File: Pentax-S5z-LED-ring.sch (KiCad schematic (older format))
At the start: 44 parts, among them IC1 ATTINY13-S, P1 CONN_2, P2 +, P3 -, P4 CONN_2, Q1 MOSFET_N, SW1 SW_PUSH, SW2 SW_PUSH

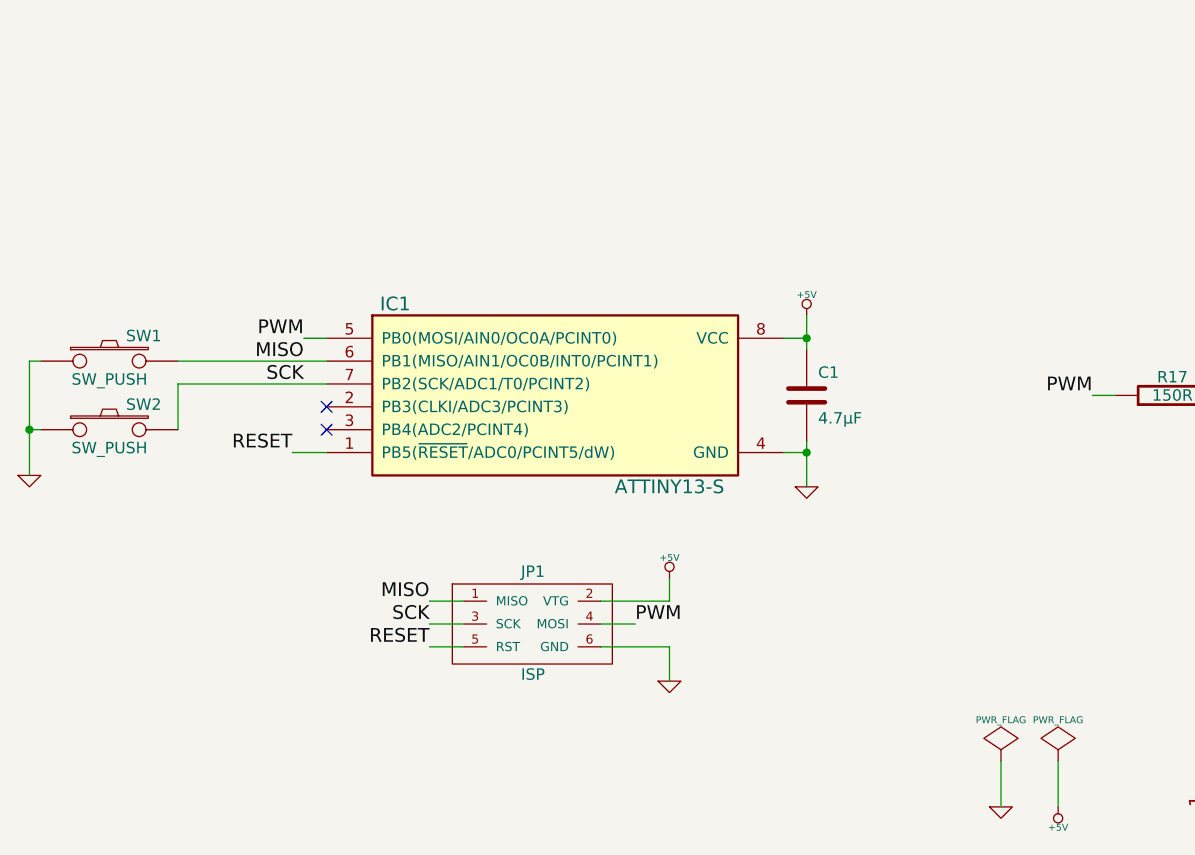
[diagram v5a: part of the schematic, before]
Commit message: Added 1k resistors for the pull-down switches. Just in case ;-)
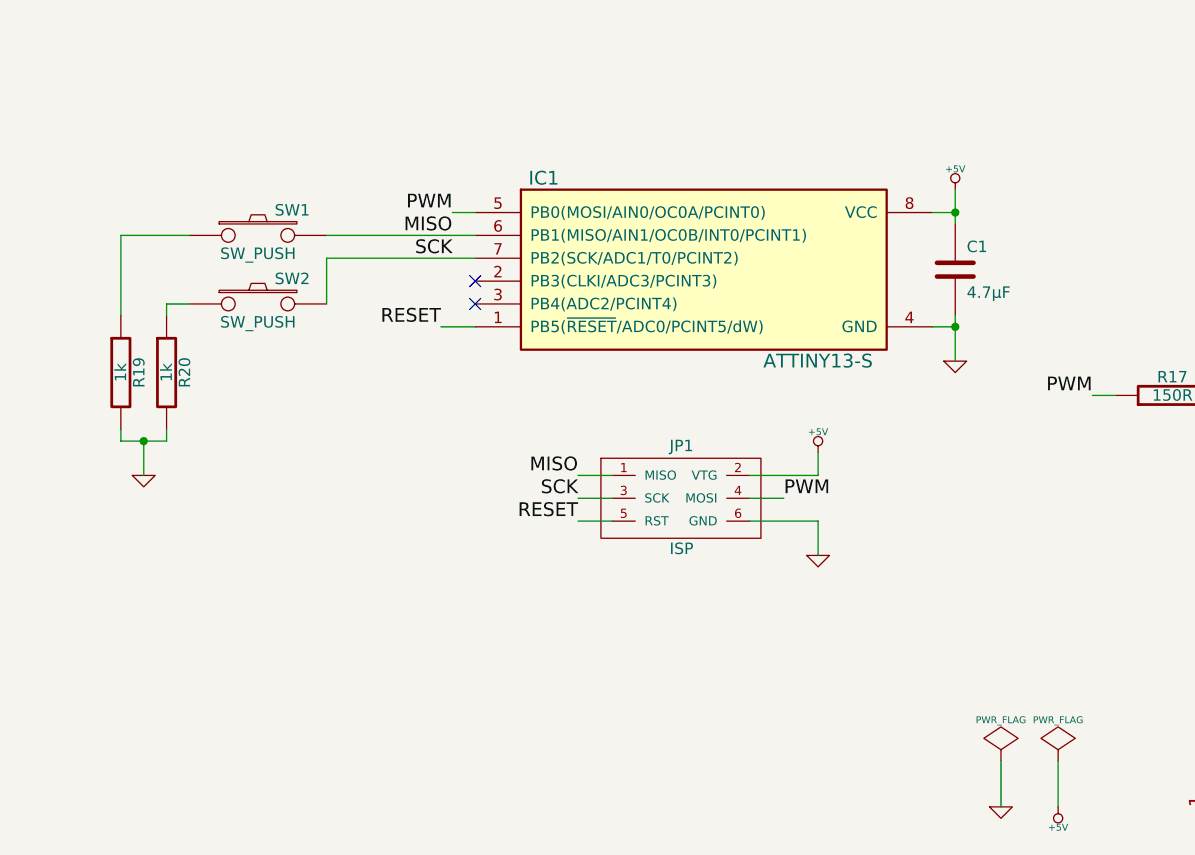
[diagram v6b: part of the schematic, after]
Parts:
- added R19, R20: 1k, symbol R
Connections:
- net GND: now also R19.2, R20.2; no longer SW1.1, SW2.1
- new net: R19.1, SW1.1
- new net: R20.1, SW2.1
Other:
- moved on the sheet: C1, IC1, JP1, SW1, SW2
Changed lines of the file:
@@
-EESchema Schematic File Version 2  date Wed 10 Apr 2013 12:16:09 AM CEST
+EESchema Schematic File Version 2  date Wed 10 Apr 2013 07:53:54 PM CEST
 LIBS:my_parts
 LIBS:power
@@
 Sheet 1 1
 Title "Pentax S5z LED ring"
-Date "9 apr 2013"
-Rev "0.1"
+Date "10 apr 2013"
+Rev "1.0"
 Comp "2013 - blog.spitzenpfeil.org"
 Comment1 ""
@@
 L ATTINY13-S IC1
 U 1 1 51640F05
-P 2500 4100
-F 0 "IC1" H 2600 4150 60  0000 C CNN
-F 1 "ATTINY13-S" H 3800 3350 60  0000 C CNN
-F 2 "SO8-200" H 2750 3350 60  0001 C CNN
-F 3 "" H 2500 4100 60  0000 C CNN
-	1    2500 4100
+P 3150 3550
+F 0 "IC1" H 3250 3600 60  0000 C CNN
+F 1 "ATTINY13-S" H 4450 2800 60  0000 C CNN
+F 2 "SO8-200" H 3400 2800 60  0001 C CNN
+F 3 "" H 3150 3550 60  0000 C CNN
+	1    3150 3550
 	1    0    0    -1
 $EndComp
@@
 L +5V #PWR04
 U 1 1 516412DB
-P 4400 4100
-F 0 "#PWR04" H 4400 4190 20  0001 C CNN
-F 1 "+5V" H 4400 4190 30  0000 C CNN
-F 2 "" H 4400 4100 60  0000 C CNN
-F 3 "" H 4400 4100 60  0000 C CNN
-	1    4400 4100
-	1    0    0    -1
-$EndComp
-Wire Wire Line
-	4400 4100 4400 4250
+P 5050 3550
+F 0 "#PWR04" H 5050 3640 20  0001 C CNN
+F 1 "+5V" H 5050 3640 30  0000 C CNN
+F 2 "" H 5050 3550 60  0000 C CNN
+F 3 "" H 5050 3550 60  0000 C CNN
+	1    5050 3550
+	1    0    0    -1
+$EndComp
+Wire Wire Line
+	5050 3550 5050 3700
 $Comp
 L GND #PWR05
 U 1 1 51641344
-P 4400 4850
-F 0 "#PWR05" H 4400 4850 30  0001 C CNN
-F 1 "GND" H 4400 4780 30  0001 C CNN
-F 2 "" H 4400 4850 60  0000 C CNN
-F 3 "" H 4400 4850 60  0000 C CNN
-	1    4400 4850
-	1    0    0    -1
-$EndComp
-Wire Wire Line
-	4400 4650 4400 4850
+P 5050 4300
+F 0 "#PWR05" H 5050 4300 30  0001 C CNN
+F 1 "GND" H 5050 4230 30  0001 C CNN
+F 2 "" H 5050 4300 60  0000 C CNN
+F 3 "" H 5050 4300 60  0000 C CNN
+	1    5050 4300
+	1    0    0    -1
+$EndComp
+Wire Wire Line
+	5050 4100 5050 4300
 Text Label 5650 4450 2    60   ~ 0
 PWM
 Wire Wire Line
 	5650 4450 5750 4450
-Text Label 2200 4200 2    60   ~ 0
+Text Label 2850 3650 2    60   ~ 0
 PWM
 Wire Wire Line
-	2200 4200 2300 4200
+	2850 3650 2950 3650
 $Comp
 L SW_PUSH SW1
 U 1 1 5164146F
-P 1350 4300
-F 0 "SW1" H 1500 4410 50  0000 C CNN
-F 1 "SW_PUSH" H 1350 4220 50  0000 C CNN
-F 2 "" H 1350 4300 60  0000 C CNN
-F 3 "" H 1350 4300 60  0000 C CNN
-	1    1350 4300
-	1    0    0    -1
-$EndComp
-$Comp
-L SW_PUSH SW2
-U 1 1 5164147E
-P 1350 4600
-F 0 "SW2" H 1500 4710 50  0000 C CNN
-F 1 "SW_PUSH" H 1350 4520 50  0000 C CNN
-F 2 "" H 1350 4600 60  0000 C CNN
-F 3 "" H 1350 4600 60  0000 C CNN
-	1    1350 4600
+P 2000 3750
+F 0 "SW1" H 2150 3860 50  0000 C CNN
+F 1 "SW_PUSH" H 2000 3670 50  0000 C CNN
+F 2 "" H 2000 3750 60  0000 C CNN
+F 3 "" H 2000 3750 60  0000 C CNN
+	1    2000 3750
 	1    0    0    -1
 $EndComp
@@
 L GND #PWR06
 U 1 1 5164148D
-P 1000 4800
-F 0 "#PWR06" H 1000 4800 30  0001 C CNN
-F 1 "GND" H 1000 4730 30  0001 C CNN
-F 2 "" H 1000 4800 60  0000 C CNN
-F 3 "" H 1000 4800 60  0000 C CNN
-	1    1000 4800
-	1    0    0    -1
-$EndComp
-Wire Wire Line
-	1050 4300 1000 4300
-Wire Wire Line
-	1000 4300 1000 4800
-Wire Wire Line
-	1000 4600 1050 4600
-Connection ~ 1000 4600
-Wire Wire Line
-	2300 4300 1650 4300
-Wire Wire Line
-	2300 4400 1650 4400
-Wire Wire Line
-	1650 4400 1650 4600
+P 1500 4800
+F 0 "#PWR06" H 1500 4800 30  0001 C CNN
+F 1 "GND" H 1500 4730 30  0001 C CNN
+F 2 "" H 1500 4800 60  0000 C CNN
+F 3 "" H 1500 4800 60  0000 C CNN
+	1    1500 4800
+	1    0    0    -1
+$EndComp
+Wire Wire Line
+	2950 3750 2300 3750
+Wire Wire Line
+	2950 3850 2300 3850
+Wire Wire Line
+	2300 3850 2300 4050
 $Comp
 L MADW__AVR_ISP JP1
 U 1 1 5164175A
-P 3200 5450
-F 0 "JP1" H 3150 5650 50  0000 L BNN
-F 1 "ISP" H 3150 5200 50  0000 L BNN
-F 2 "~" H 3200 5450 60  0000 C CNN
-F 3 "~" H 3200 5450 60  0000 C CNN
-	1    3200 5450
-	1    0    0    -1
-$EndComp
-Wire Wire Line
-	2900 5350 2750 5350
-Wire Wire Line
-	2750 5450 2900 5450
-Wire Wire Line
-	2900 5550 2750 5550
-Wire Wire Line
-	3500 5350 3800 5350
-Wire Wire Line
-	3500 5450 3650 5450
-Wire Wire Line
-	3500 5550 3800 5550
+P 3850 4900
+F 0 "JP1" H 3800 5100 50  0000 L BNN
+F 1 "ISP" H 3800 4650 50  0000 L BNN
+F 2 "~" H 3850 4900 60  0000 C CNN
+F 3 "~" H 3850 4900 60  0000 C CNN
+	1    3850 4900
+	1    0    0    -1
+$EndComp
+Wire Wire Line
+	3550 4800 3400 4800
+Wire Wire Line
+	3400 4900 3550 4900
+Wire Wire Line
+	3550 5000 3400 5000
+Wire Wire Line
+	4150 4800 4450 4800
+Wire Wire Line
+	4150 4900 4300 4900
+Wire Wire Line
+	4150 5000 4450 5000
 $Comp
 L GND #PWR07
 U 1 1 516419E6
-P 3800 5700
-F 0 "#PWR07" H 3800 5700 30  0001 C CNN
-F 1 "GND" H 3800 5630 30  0001 C CNN
-F 2 "" H 3800 5700 60  0000 C CNN
-F 3 "" H 3800 5700 60  0000 C CNN
-	1    3800 5700
+P 4450 5150
+F 0 "#PWR07" H 4450 5150 30  0001 C CNN
+F 1 "GND" H 4450 5080 30  0001 C CNN
+F 2 "" H 4450 5150 60  0000 C CNN
+F 3 "" H 4450 5150 60  0000 C CNN
+	1    4450 5150
 	1    0    0    -1
 $EndComp
@@
 L +5V #PWR08
 U 1 1 516419F5
-P 3800 5250
-F 0 "#PWR08" H 3800 5340 20  0001 C CNN
-F 1 "+5V" H 3800 5340 30  0000 C CNN
-F 2 "" H 3800 5250 60  0000 C CNN
-F 3 "" H 3800 5250 60  0000 C CNN
-	1    3800 5250
-	1    0    0    -1
-$EndComp
-Wire Wire Line
-	3800 5350 3800 5250
-Wire Wire Line
-	3800 5550 3800 5700
-Text Label 3650 5450 0    60   ~ 0
+P 4450 4700
+F 0 "#PWR08" H 4450 4790 20  0001 C CNN
+F 1 "+5V" H 4450 4790 30  0000 C CNN
+F 2 "" H 4450 4700 60  0000 C CNN
+F 3 "" H 4450 4700 60  0000 C CNN
+	1    4450 4700
+	1    0    0    -1
+$EndComp
+Wire Wire Line
+	4450 4800 4450 4700
+Wire Wire Line
+	4450 5000 4450 5150
+Text Label 4300 4900 0    60   ~ 0
 PWM
-Text Label 2750 5350 2    60   ~ 0
+Text Label 3400 4800 2    60   ~ 0
 MISO
-Text Label 2750 5450 2    60   ~ 0
+Text Label 3400 4900 2    60   ~ 0
 SCK
-Text Label 2750 5550 2    60   ~ 0
+Text Label 3400 5000 2    60   ~ 0
 RESET
-Text Label 2200 4300 2    60   ~ 0
+Text Label 2850 3750 2    60   ~ 0
 MISO
-Text Label 2200 4400 2    60   ~ 0
+Text Label 2850 3850 2    60   ~ 0
 SCK
-Text Label 2150 4700 2    60   ~ 0
+Text Label 2800 4150 2    60   ~ 0
 RESET
 Wire Wire Line
-	2150 4700 2300 4700
-NoConn ~ 2300 4500
-NoConn ~ 2300 4600
+	2800 4150 2950 4150
+NoConn ~ 2950 3950
+NoConn ~ 2950 4050
 $Comp
 L GND #PWR09
@@
 Text Notes 7150 3850 0    60   ~ 0
 To LED board
-Connection ~ 4400 4200
-Connection ~ 4400 4700
+Connection ~ 5050 3650
+Connection ~ 5050 4150
 $Comp
 L C C1
 U 1 1 516492F3
-P 4400 4450
-F 0 "C1" H 4450 4550 50  0000 L CNN
-F 1 "4.7µF" H 4450 4350 50  0000 L CNN
-F 2 "" H 4400 4450 60  0000 C CNN
-F 3 "" H 4400 4450 60  0000 C CNN
-	1    4400 4450
-	1    0    0    -1
-$EndComp
-Wire Wire Line
-	4300 4200 4400 4200
-Wire Wire Line
-	4300 4700 4400 4700
+P 5050 3900
+F 0 "C1" H 5100 4000 50  0000 L CNN
+F 1 "4.7µF" H 5100 3800 50  0000 L CNN
+F 2 "" H 5050 3900 60  0000 C CNN
+F 3 "" H 5050 3900 60  0000 C CNN
+	1    5050 3900
+	1    0    0    -1
+$EndComp
+Wire Wire Line
+	4950 3650 5050 3650
+Wire Wire Line
+	4950 4150 5050 4150
+$Comp
+L R R19
+U 1 1 5165A46F
+P 1400 4350
+F 0 "R19" V 1480 4350 50  0000 C CNN
+F 1 "1k" V 1400 4350 50  0000 C CNN
+F 2 "" H 1400 4350 60  0000 C CNN
+F 3 "" H 1400 4350 60  0000 C CNN
+	1    1400 4350
+	1    0    0    -1
+$EndComp
+$Comp
+L R R20
+U 1 1 5165A47E
+P 1600 4350
+F 0 "R20" V 1680 4350 50  0000 C CNN
+F 1 "1k" V 1600 4350 50  0000 C CNN
+F 2 "" H 1600 4350 60  0000 C CNN
+F 3 "" H 1600 4350 60  0000 C CNN
+	1    1600 4350
+	1    0    0    -1
+$EndComp
+$Comp
+L SW_PUSH SW2
+U 1 1 5164147E
+P 2000 4050
+F 0 "SW2" H 2150 4160 50  0000 C CNN
+F 1 "SW_PUSH" H 2000 3970 50  0000 C CNN
+F 2 "" H 2000 4050 60  0000 C CNN
+F 3 "" H 2000 4050 60  0000 C CNN
+	1    2000 4050
+	1    0    0    -1
+$EndComp
+Wire Wire Line
+	1700 3750 1400 3750
+Wire Wire Line
+	1400 3750 1400 4100
+Wire Wire Line
+	1600 4100 1600 4050
+Wire Wire Line
+	1600 4050 1700 4050
+Wire Wire Line
+	1400 4600 1400 4650
+Wire Wire Line
+	1400 4650 1600 4650
+Wire Wire Line
+	1600 4650 1600 4600
+Wire Wire Line
+	1500 4650 1500 4800
+Connection ~ 1500 4650
 $EndSCHEMATC

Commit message: Changed the LED dropper resistors to 65R + added some text.
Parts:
- R1: value 60R -> 65R
- R10, R11, R12, R13, R14, R15, R16, R2, R3, R4, R5, R6, R7, R8, R9: value 10R -> 65R
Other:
- note added: "WW: 3.29V --> 26mA --> 65R (5V)\n W: 3.19V --> 28mA --> 65R (5V)"
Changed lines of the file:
@@
-EESchema Schematic File Version 2  date Wed 10 Apr 2013 07:53:54 PM CEST
+EESchema Schematic File Version 2  date Mon 29 Apr 2013 01:08:56 AM CEST
 LIBS:my_parts
 LIBS:power
@@
 Sheet 1 1
 Title "Pentax S5z LED ring"
-Date "10 apr 2013"
+Date "28 apr 2013"
 Rev "1.0"
 Comp "2013 - blog.spitzenpfeil.org"
@@
 P 6300 1850
 F 0 "R1" V 6380 1850 50  0000 C CNN
-F 1 "60R" V 6300 1850 50  0000 C CNN
+F 1 "65R" V 6300 1850 50  0000 C CNN
 F 2 "" H 6300 1850 60  0000 C CNN
 F 3 "" H 6300 1850 60  0000 C CNN
@@
 P 6600 1850
 F 0 "R2" V 6680 1850 50  0000 C CNN
-F 1 "10R" V 6600 1850 50  0000 C CNN
+F 1 "65R" V 6600 1850 50  0000 C CNN
 F 2 "" H 6600 1850 60  0000 C CNN
 F 3 "" H 6600 1850 60  0000 C CNN
@@
 P 6900 1850
 F 0 "R3" V 6980 1850 50  0000 C CNN
-F 1 "10R" V 6900 1850 50  0000 C CNN
+F 1 "65R" V 6900 1850 50  0000 C CNN
 F 2 "" H 6900 1850 60  0000 C CNN
 F 3 "" H 6900 1850 60  0000 C CNN
@@
 P 7200 1850
 F 0 "R4" V 7280 1850 50  0000 C CNN
-F 1 "10R" V 7200 1850 50  0000 C CNN
+F 1 "65R" V 7200 1850 50  0000 C CNN
 F 2 "" H 7200 1850 60  0000 C CNN
 F 3 "" H 7200 1850 60  0000 C CNN
@@
 P 7500 1850
 F 0 "R5" V 7580 1850 50  0000 C CNN
-F 1 "10R" V 7500 1850 50  0000 C CNN
+F 1 "65R" V 7500 1850 50  0000 C CNN
 F 2 "" H 7500 1850 60  0000 C CNN
 F 3 "" H 7500 1850 60  0000 C CNN
@@
 P 7800 1850
 F 0 "R6" V 7880 1850 50  0000 C CNN
-F 1 "10R" V 7800 1850 50  0000 C CNN
+F 1 "65R" V 7800 1850 50  0000 C CNN
 F 2 "" H 7800 1850 60  0000 C CNN
 F 3 "" H 7800 1850 60  0000 C CNN
@@
 P 8100 1850
 F 0 "R7" V 8180 1850 50  0000 C CNN
-F 1 "10R" V 8100 1850 50  0000 C CNN
+F 1 "65R" V 8100 1850 50  0000 C CNN
 F 2 "" H 8100 1850 60  0000 C CNN
 F 3 "" H 8100 1850 60  0000 C CNN
@@
 P 8400 1850
 F 0 "R8" V 8480 1850 50  0000 C CNN
-F 1 "10R" V 8400 1850 50  0000 C CNN
+F 1 "65R" V 8400 1850 50  0000 C CNN
 F 2 "" H 8400 1850 60  0000 C CNN
 F 3 "" H 8400 1850 60  0000 C CNN
@@
 P 8700 1850
 F 0 "R9" V 8780 1850 50  0000 C CNN
-F 1 "10R" V 8700 1850 50  0000 C CNN
+F 1 "65R" V 8700 1850 50  0000 C CNN
 F 2 "" H 8700 1850 60  0000 C CNN
 F 3 "" H 8700 1850 60  0000 C CNN
@@
 P 9000 1850
 F 0 "R10" V 9080 1850 50  0000 C CNN
-F 1 "10R" V 9000 1850 50  0000 C CNN
+F 1 "65R" V 9000 1850 50  0000 C CNN
 F 2 "" H 9000 1850 60  0000 C CNN
 F 3 "" H 9000 1850 60  0000 C CNN
@@
 P 9300 1850
 F 0 "R11" V 9380 1850 50  0000 C CNN
-F 1 "10R" V 9300 1850 50  0000 C CNN
+F 1 "65R" V 9300 1850 50  0000 C CNN
 F 2 "" H 9300 1850 60  0000 C CNN
 F 3 "" H 9300 1850 60  0000 C CNN
@@
 P 9600 1850
 F 0 "R12" V 9680 1850 50  0000 C CNN
-F 1 "10R" V 9600 1850 50  0000 C CNN
+F 1 "65R" V 9600 1850 50  0000 C CNN
 F 2 "" H 9600 1850 60  0000 C CNN
 F 3 "" H 9600 1850 60  0000 C CNN
@@
 P 9900 1850
 F 0 "R13" V 9980 1850 50  0000 C CNN
-F 1 "10R" V 9900 1850 50  0000 C CNN
+F 1 "65R" V 9900 1850 50  0000 C CNN
 F 2 "" H 9900 1850 60  0000 C CNN
 F 3 "" H 9900 1850 60  0000 C CNN
@@
 P 10200 1850
 F 0 "R14" V 10280 1850 50  0000 C CNN
-F 1 "10R" V 10200 1850 50  0000 C CNN
+F 1 "65R" V 10200 1850 50  0000 C CNN
 F 2 "" H 10200 1850 60  0000 C CNN
 F 3 "" H 10200 1850 60  0000 C CNN
@@
 P 10500 1850
 F 0 "R15" V 10580 1850 50  0000 C CNN
-F 1 "10R" V 10500 1850 50  0000 C CNN
+F 1 "65R" V 10500 1850 50  0000 C CNN
 F 2 "" H 10500 1850 60  0000 C CNN
 F 3 "" H 10500 1850 60  0000 C CNN
@@
 P 10800 1850
 F 0 "R16" V 10880 1850 50  0000 C CNN
-F 1 "10R" V 10800 1850 50  0000 C CNN
+F 1 "65R" V 10800 1850 50  0000 C CNN
 F 2 "" H 10800 1850 60  0000 C CNN
 F 3 "" H 10800 1850 60  0000 C CNN
@@
 Connection ~ 8550 1050
 $Comp
-L +5V #PWR04
+L +5V #PWR03
 U 1 1 516412DB
 P 5050 3550
-F 0 "#PWR04" H 5050 3640 20  0001 C CNN
+F 0 "#PWR03" H 5050 3640 20  0001 C CNN
 F 1 "+5V" H 5050 3640 30  0000 C CNN
 F 2 "" H 5050 3550 60  0000 C CNN
@@
 	5050 3550 5050 3700
 $Comp
-L GND #PWR05
+L GND #PWR04
 U 1 1 51641344
 P 5050 4300
-F 0 "#PWR05" H 5050 4300 30  0001 C CNN
+F 0 "#PWR04" H 5050 4300 30  0001 C CNN
 F 1 "GND" H 5050 4230 30  0001 C CNN
 F 2 "" H 5050 4300 60  0000 C CNN
@@
 $EndComp
 $Comp
-L GND #PWR06
+L GND #PWR05
 U 1 1 5164148D
 P 1500 4800
-F 0 "#PWR06" H 1500 4800 30  0001 C CNN
+F 0 "#PWR05" H 1500 4800 30  0001 C CNN
 F 1 "GND" H 1500 4730 30  0001 C CNN
 F 2 "" H 1500 4800 60  0000 C CNN
@@
 	4150 5000 4450 5000
 $Comp
-L GND #PWR07
+L GND #PWR06
 U 1 1 516419E6
 P 4450 5150
-F 0 "#PWR07" H 4450 5150 30  0001 C CNN
+F 0 "#PWR06" H 4450 5150 30  0001 C CNN
 F 1 "GND" H 4450 5080 30  0001 C CNN
 F 2 "" H 4450 5150 60  0000 C CNN
@@
 $EndComp
 $Comp
-L +5V #PWR08
+L +5V #PWR07
 U 1 1 516419F5
 P 4450 4700
-F 0 "#PWR08" H 4450 4790 20  0001 C CNN
+F 0 "#PWR07" H 4450 4790 20  0001 C CNN
 F 1 "+5V" H 4450 4790 30  0000 C CNN
 F 2 "" H 4450 4700 60  0000 C CNN
@@
 NoConn ~ 2950 4050
 $Comp
-L GND #PWR09
+L GND #PWR08
 U 1 1 51644384
 P 5250 6250
-F 0 "#PWR09" H 5250 6250 30  0001 C CNN
+F 0 "#PWR08" H 5250 6250 30  0001 C CNN
 F 1 "GND" H 5250 6180 30  0001 C CNN
 F 2 "" H 5250 6250 60  0000 C CNN
@@
 $EndComp
 $Comp
-L +5V #PWR010
+L +5V #PWR09
 U 1 1 51644393
 P 5500 6250
-F 0 "#PWR010" H 5500 6340 20  0001 C CNN
+F 0 "#PWR09" H 5500 6340 20  0001 C CNN
 F 1 "+5V" H 5500 6340 30  0000 C CNN
 F 2 "" H 5500 6250 60  0000 C CNN
@@
 $EndComp
 $Comp
-L PWR_FLAG #FLG011
+L PWR_FLAG #FLG010
 U 1 1 516443A2
 P 5250 6050
-F 0 "#FLG011" H 5250 6145 30  0001 C CNN
+F 0 "#FLG010" H 5250 6145 30  0001 C CNN
 F 1 "PWR_FLAG" H 5250 6230 30  0000 C CNN
 F 2 "" H 5250 6050 60  0000 C CNN
@@
 $EndComp
 $Comp
-L PWR_FLAG #FLG012
+L PWR_FLAG #FLG011
 U 1 1 516443B1
 P 5500 6050
-F 0 "#FLG012" H 5500 6145 30  0001 C CNN
+F 0 "#FLG011" H 5500 6145 30  0001 C CNN
 F 1 "PWR_FLAG" H 5500 6230 30  0000 C CNN
 F 2 "" H 5500 6050 60  0000 C CNN
@@
 $EndComp
 $Comp
-L GND #PWR013
+L GND #PWR012
 U 1 1 51646D84
 P 6350 6450
-F 0 "#PWR013" H 6350 6450 30  0001 C CNN
+F 0 "#PWR012" H 6350 6450 30  0001 C CNN
 F 1 "GND" H 6350 6380 30  0001 C CNN
 F 2 "" H 6350 6450 60  0000 C CNN
@@
 $EndComp
 $Comp
-L +5V #PWR014
+L +5V #PWR013
 U 1 1 51646D93
 P 6150 6450
-F 0 "#PWR014" H 6150 6540 20  0001 C CNN
+F 0 "#PWR013" H 6150 6540 20  0001 C CNN
 F 1 "+5V" H 6150 6540 30  0000 C CNN
 F 2 "" H 6150 6450 60  0000 C CNN
@@
 	6650 3900 6650 4150
 $Comp
-L +5V #PWR?
+L +5V #PWR014
 U 1 1 516472A6
 P 6650 3650
-F 0 "#PWR?" H 6650 3740 20  0001 C CNN
+F 0 "#PWR014" H 6650 3740 20  0001 C CNN
 F 1 "+5V" H 6650 3740 30  0000 C CNN
 F 2 "" H 6650 3650 60  0000 C CNN
@@
 	1500 4650 1500 4800
 Connection ~ 1500 4650
+Text Notes 4250 1550 0    60   ~ 0
+WW: 3.29V --> 26mA --> 65R (5V)\n  W: 3.19V --> 28mA -->  65R (5V)
 $EndSCHEMATC
